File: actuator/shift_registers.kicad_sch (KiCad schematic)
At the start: 3 parts, among them U1 HV509, U2 HV509

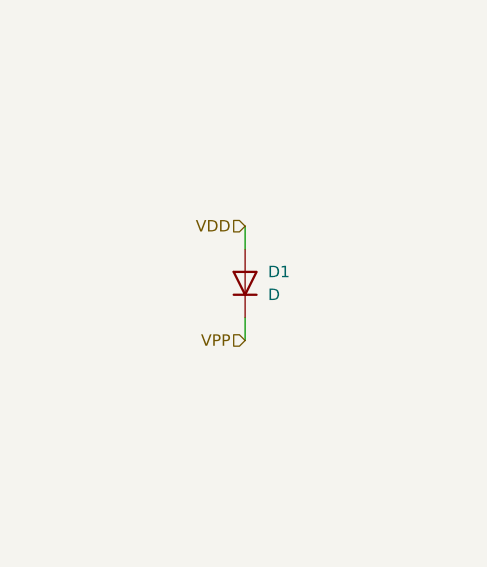
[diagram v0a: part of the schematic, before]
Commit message: actuator: add capacitor for vdd, no exposed copper on backside
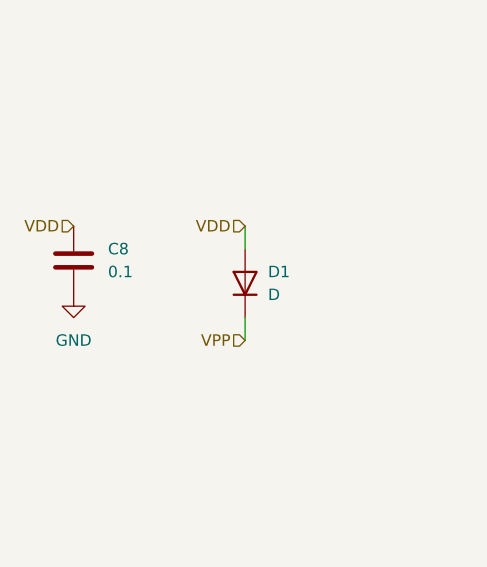
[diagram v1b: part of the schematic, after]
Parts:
- added C8: 0.1, Capacitor_SMD:C_0603_1608Metric, symbol Device:C
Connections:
- net GND: now also C8.2
- net VDD: now also C8.1
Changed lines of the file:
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@@
+    (effects (font (size 1.27 1.27)) (justify right))
+  )
+  (hierarchical_label "VDD" (shape input) (at 62.23 85.09 180) (fields_autoplaced)
     (effects (font (size 1.27 1.27)) (justify right))
   )
@@
     )
   )
+  (symbol (lib_name "GND_1") (lib_id "power:GND") (at 62.23 92.71 0) (unit 1)
+    (in_bom yes) (on_board yes) (dnp no) (fields_autoplaced)
+    (property "Reference" "#PWR05" (at 62.23 99.06 0)
+      (effects (font (size 1.27 1.27)) hide)
+    )
+    (property "Value" "GND" (at 62.23 97.79 0)
+      (effects (font (size 1.27 1.27)))
+    )
+    (property "Footprint" "" (at 62.23 92.71 0)
+      (effects (font (size 1.27 1.27)) hide)
+    )
+    (property "Datasheet" "" (at 62.23 92.71 0)
+      (effects (font (size 1.27 1.27)) hide)
+    )
+    (pin "1")
+    (instances
+      (project "actuator"
+        (path "/e63e39d7-6ac0-4ffd-8aa3-1841a4541b55/488f8d40-8ebd-4514-a509-75fe26050312"
+          (reference "#PWR05") (unit 1)
+        )
+      )
+    )
+  )
   (symbol (lib_id "power:GND") (at 138.43 91.44 0) (unit 1)
     (in_bom yes) (on_board yes) (dnp no)
@@
         )
       )
+    )
+  )
+  (symbol (lib_id "Device:C") (at 62.23 88.9 0) (unit 1)
+    (in_bom yes) (on_board yes) (dnp no) (fields_autoplaced)
+    (property "Reference" "C8" (at 66.04 87.63 0)
+      (effects (font (size 1.27 1.27)) (justify left))
+    )
+    (property "Value" "0.1" (at 66.04 90.17 0)
+      (effects (font (size 1.27 1.27)) (justify left))
+    )
+    (property "Footprint" "Capacitor_SMD:C_0603_1608Metric" (at 63.1952 92.71 0)
+      (effects (font (size 1.27 1.27)) hide)
+    )
+    (property "Datasheet" "~" (at 62.23 88.9 0)
+      (effects (font (size 1.27 1.27)) hide)
+    )
+    (pin "1")
+    (pin "2")
+    (instances
+      (project "actuator"
+        (path "/e63e39d7-6ac0-4ffd-8aa3-1841a4541b55/488f8d40-8ebd-4514-a509-75fe26050312"
+          (reference "C8") (unit 1)
+        )
+      )

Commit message: actuator ibom
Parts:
- C8: value 0.1 -> 0.1 µF
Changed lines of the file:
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@@
       (effects (font (size 1.27 1.27)) (justify left))
     )
-    (property "Value" "0.1" (at 66.04 90.17 0)
+    (property "Value" "0.1 µF" (at 66.04 90.17 0)
       (effects (font (size 1.27 1.27)) (justify left))
     )

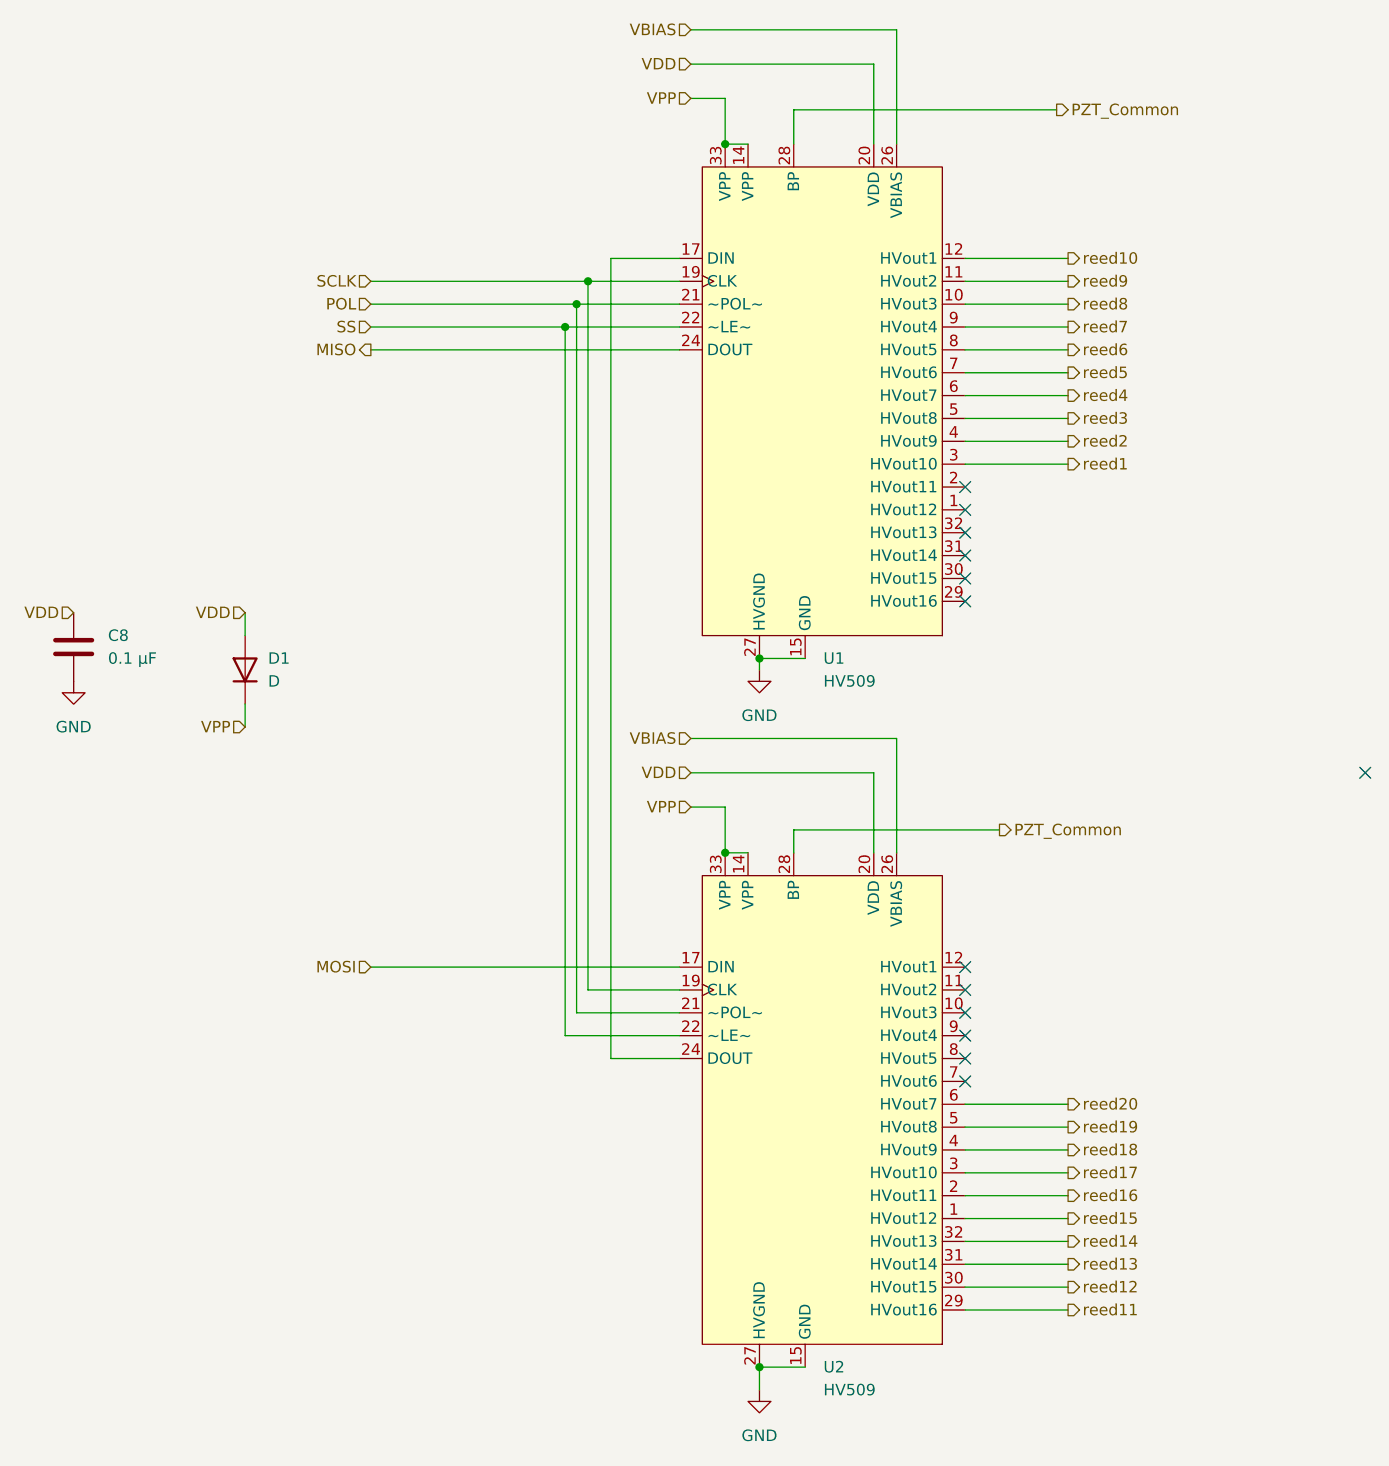
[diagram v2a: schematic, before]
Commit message: actuator move testpoints to subsheets
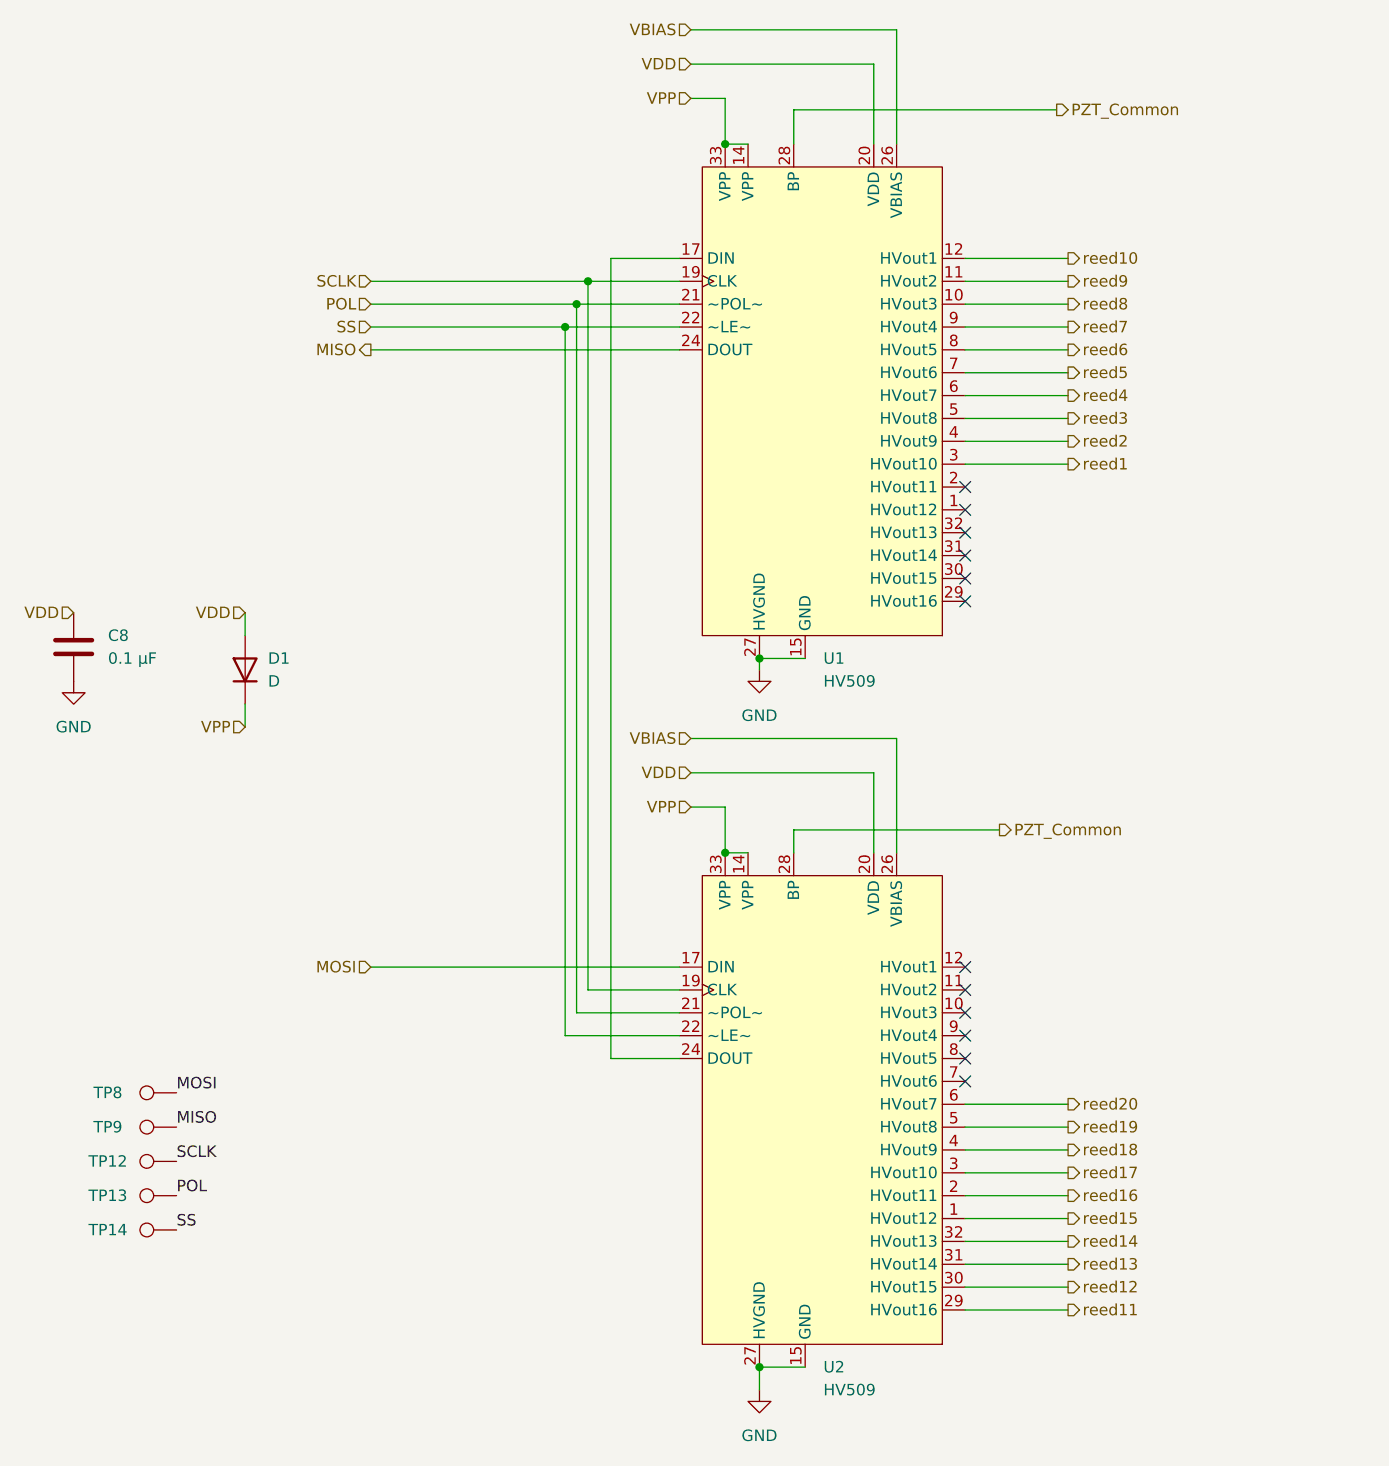
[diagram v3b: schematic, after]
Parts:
- added TP12, TP13, TP14, TP8, TP9: TestPoint, TestPoint:TestPoint_THTPad_D1.0mm_Drill0.5mm, symbol Connector:TestPoint
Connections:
- net MISO: now also TP9.1
- net MOSI: now also TP8.1
- net POL: now also TP13.1
- net SCLK: now also TP12.1
- net SS: now also TP14.1
- no-connect marks 13 -> 12
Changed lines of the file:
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@@
   (no_connect (at 161.29 124.46))
   (no_connect (at 161.29 132.08))
-  (no_connect (at 205.74 102.87))
   (no_connect (at 161.29 73.66))
   (no_connect (at 161.29 83.82))
@@
     (stroke (width 0) (type default))
   )
+  (label "SS" (at 73.66 153.67 0) (fields_autoplaced)
+    (effects (font (size 1.27 1.27)) (justify left bottom))
+  )
+  (label "POL" (at 73.66 149.86 0) (fields_autoplaced)
+    (effects (font (size 1.27 1.27)) (justify left bottom))
+  )
+  (label "SCLK" (at 73.66 146.05 0) (fields_autoplaced)
+    (effects (font (size 1.27 1.27)) (justify left bottom))
+  )
+  (label "MOSI" (at 73.66 138.43 0) (fields_autoplaced)
+    (effects (font (size 1.27 1.27)) (justify left bottom))
+  )
+  (label "MISO" (at 73.66 142.24 0) (fields_autoplaced)
+    (effects (font (size 1.27 1.27)) (justify left bottom))
+  )
   (hierarchical_label "reed2" (shape output) (at 172.72 66.04 0) (fields_autoplaced)
     (effects (font (size 1.27 1.27)) (justify left))
@@
   (hierarchical_label "MOSI" (shape input) (at 95.25 124.46 180) (fields_autoplaced)
     (effects (font (size 1.27 1.27)) (justify right))
+  )
+  (symbol (lib_id "Connector:TestPoint") (at 73.66 138.43 90) (unit 1)
+    (in_bom yes) (on_board yes) (dnp no)
+    (property "Reference" "TP8" (at 66.04 138.43 90)
+      (effects (font (size 1.27 1.27)))
+    )
+    (property "Value" "TestPoint" (at 80.01 138.43 90)
+      (effects (font (size 1.27 1.27)) hide)
+    )
+    (property "Footprint" "TestPoint:TestPoint_THTPad_D1.0mm_Drill0.5mm" (at 73.66 133.35 0)
+      (effects (font (size 1.27 1.27)) hide)
+    )
+    (property "Datasheet" "~" (at 73.66 133.35 0)
+      (effects (font (size 1.27 1.27)) hide)
+    )
+    (pin "1")
+    (instances
+      (project "actuator"
+        (path "/e63e39d7-6ac0-4ffd-8aa3-1841a4541b55"
+          (reference "TP8") (unit 1)
+        )
+        (path "/e63e39d7-6ac0-4ffd-8aa3-1841a4541b55/488f8d40-8ebd-4514-a509-75fe26050312"
+          (reference "TP8") (unit 1)
+        )
+      )
+    )
   )
   (symbol (lib_id "Device:D") (at 81.28 91.44 90) (unit 1)
@@
     )
   )
+  (symbol (lib_id "Connector:TestPoint") (at 73.66 146.05 90) (unit 1)
+    (in_bom yes) (on_board yes) (dnp no)
+    (property "Reference" "TP12" (at 66.04 146.05 90)
+      (effects (font (size 1.27 1.27)))
+    )
+    (property "Value" "TestPoint" (at 80.01 146.05 90)
+      (effects (font (size 1.27 1.27)) hide)
+    )
+    (property "Footprint" "TestPoint:TestPoint_THTPad_D1.0mm_Drill0.5mm" (at 73.66 140.97 0)
+      (effects (font (size 1.27 1.27)) hide)
+    )
+    (property "Datasheet" "~" (at 73.66 140.97 0)
+      (effects (font (size 1.27 1.27)) hide)
+    )
+    (pin "1")
+    (instances
+      (project "actuator"
+        (path "/e63e39d7-6ac0-4ffd-8aa3-1841a4541b55"
+          (reference "TP12") (unit 1)
+        )
+        (path "/e63e39d7-6ac0-4ffd-8aa3-1841a4541b55/488f8d40-8ebd-4514-a509-75fe26050312"
+          (reference "TP12") (unit 1)
+        )
+      )
+    )
+  )
   (symbol (lib_id "power:GND") (at 138.43 91.44 0) (unit 1)
     (in_bom yes) (on_board yes) (dnp no)
@@
     )
   )
+  (symbol (lib_id "Connector:TestPoint") (at 73.66 149.86 90) (unit 1)
+    (in_bom yes) (on_board yes) (dnp no)
+    (property "Reference" "TP13" (at 66.04 149.86 90)
+      (effects (font (size 1.27 1.27)))
+    )
+    (property "Value" "TestPoint" (at 80.01 149.86 90)
+      (effects (font (size 1.27 1.27)) hide)
+    )
+    (property "Footprint" "TestPoint:TestPoint_THTPad_D1.0mm_Drill0.5mm" (at 73.66 144.78 0)
+      (effects (font (size 1.27 1.27)) hide)
+    )
+    (property "Datasheet" "~" (at 73.66 144.78 0)
+      (effects (font (size 1.27 1.27)) hide)
+    )
+    (pin "1")
+    (instances
+      (project "actuator"
+        (path "/e63e39d7-6ac0-4ffd-8aa3-1841a4541b55"
+          (reference "TP13") (unit 1)
+        )
+        (path "/e63e39d7-6ac0-4ffd-8aa3-1841a4541b55/488f8d40-8ebd-4514-a509-75fe26050312"
+          (reference "TP13") (unit 1)
+        )
+      )
+    )
+  )
   (symbol (lib_id "Device:C") (at 62.23 88.9 0) (unit 1)
     (in_bom yes) (on_board yes) (dnp no) (fields_autoplaced)
@@
         )
       )
+    )
+  )
+  (symbol (lib_id "Connector:TestPoint") (at 73.66 142.24 90) (unit 1)
+    (in_bom yes) (on_board yes) (dnp no)
+    (property "Reference" "TP9" (at 66.04 142.24 90)
+      (effects (font (size 1.27 1.27)))
+    )
+    (property "Value" "TestPoint" (at 80.01 142.24 90)
+      (effects (font (size 1.27 1.27)) hide)
+    )
+    (property "Footprint" "TestPoint:TestPoint_THTPad_D1.0mm_Drill0.5mm" (at 73.66 137.16 0)
+      (effects (font (size 1.27 1.27)) hide)
+    )
+    (property "Datasheet" "~" (at 73.66 137.16 0)
+      (effects (font (size 1.27 1.27)) hide)
+    )
+    (pin "1")
+    (instances
+      (project "actuator"
+        (path "/e63e39d7-6ac0-4ffd-8aa3-1841a4541b55"
+          (reference "TP9") (unit 1)
+        )
+        (path "/e63e39d7-6ac0-4ffd-8aa3-1841a4541b55/488f8d40-8ebd-4514-a509-75fe26050312"
+          (reference "TP9") (unit 1)
+        )
+      )
+    )
+  )
+  (symbol (lib_id "Connector:TestPoint") (at 73.66 153.67 90) (unit 1)
+    (in_bom yes) (on_board yes) (dnp no)
+    (property "Reference" "TP14" (at 66.04 153.67 90)
+      (effects (font (size 1.27 1.27)))
+    )
+    (property "Value" "TestPoint" (at 80.01 153.67 90)
+      (effects (font (size 1.27 1.27)) hide)
+    )
+    (property "Footprint" "TestPoint:TestPoint_THTPad_D1.0mm_Drill0.5mm" (at 73.66 148.59 0)
+      (effects (font (size 1.27 1.27)) hide)
+    )
+    (property "Datasheet" "~" (at 73.66 148.59 0)
+      (effects (font (size 1.27 1.27)) hide)
+    )
+    (pin "1")
+    (instances
+      (project "actuator"
+        (path "/e63e39d7-6ac0-4ffd-8aa3-1841a4541b55"
+          (reference "TP14") (unit 1)
+        )
+        (path "/e63e39d7-6ac0-4ffd-8aa3-1841a4541b55/488f8d40-8ebd-4514-a509-75fe26050312"
+          (reference "TP14") (unit 1)
+        )
+      )
